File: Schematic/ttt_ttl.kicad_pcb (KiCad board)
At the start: 2 copper layers, 79.8 x 129.5 mm, 80 parts, among them J1 Conn_01x01, J2 Conn_01x01, SW1 SW_Push, SW10 SW_Push, SW2 SW_Push, SW3 SW_Push, SW4 SW_Push, SW5 SW_Push, SW6 SW_Push, SW7 SW_Push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

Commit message: Thanks to Ken Yap, I modified the project to optionally allow the board to move first.
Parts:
- added R13: 10K, Resistor_THT:R_Axial_DIN0207_L6.3mm_D2.5mm_P7.62mm_Horizontal, F.Cu at (101.5, 120.9)
- added SW11: DPDTx2, Package_DIP:DIP-6_W7.62mm, F.Cu at (94.3, 112.6)
- moved R37 4.16 mm to (94.1, 139.1)
- moved D19 4.15 mm to (100.6, 135.4)
- moved D20 3.90 mm to (94.9, 135.4)
- moved R38 3.44 mm to (94.0, 142.5)
- moved U11 3.19 mm to (93.7, 121.0)
- moved C2 2.86 mm to (100.1, 146.0)
- moved R41 2.74 mm to (94.7, 146.0)
- moved U13 2.42 mm to (67.9, 139.0)
- moved C1 1.61 mm to (89.9, 150.9)
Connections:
- U10 pad 26: Lo -> Net-(R13-Pad2)
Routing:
- net Net-(R13-Pad2): track 0.00 -> 61.4 mm
- net Move1: track 123.9 -> 176.3 mm
- net User9: track 72.4 -> 94.9 mm, vias 1 -> 0
- net Newstate3: track 30.8 -> 51.1 mm, vias 1 -> 0
- net Net-(U10-Pad18): track 63.3 -> 45.5 mm
- net Clk: track 362.0 -> 378.6 mm
- net Move4: track 104.8 -> 92.2 mm, vias 0 -> 1
- net Hi: track 582.0 -> 594.5 mm
- net Reset: track 400.0 -> 388.3 mm
- net Move7: track 51.5 -> 62.8 mm, vias 0 -> 1
- net Net-(R38-Pad1): track 24.1 -> 33.3 mm
- net Move2: track 114.4 -> 105.6 mm
- net User3: track 139.4 -> 132.2 mm
- net Newstate0: track 28.3 -> 33.6 mm
- net Net-(R4-Pad1): track 34.1 -> 28.8 mm
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
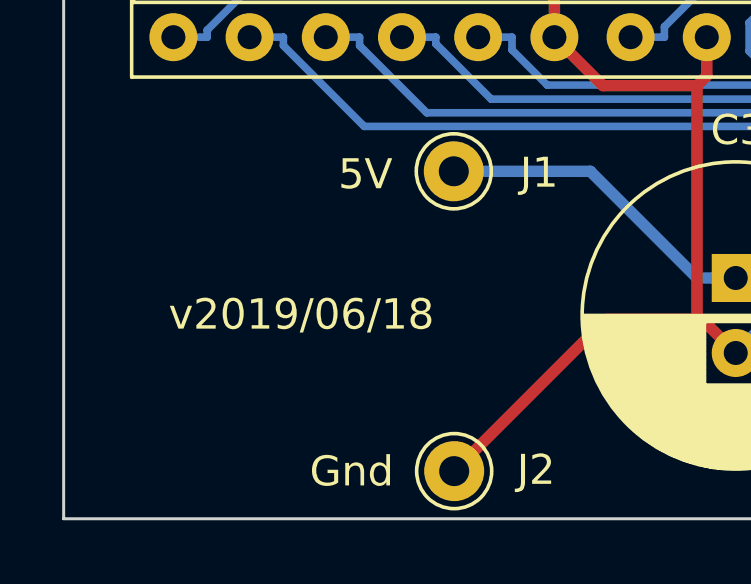
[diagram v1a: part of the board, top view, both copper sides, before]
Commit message: Updated the PCB version number.
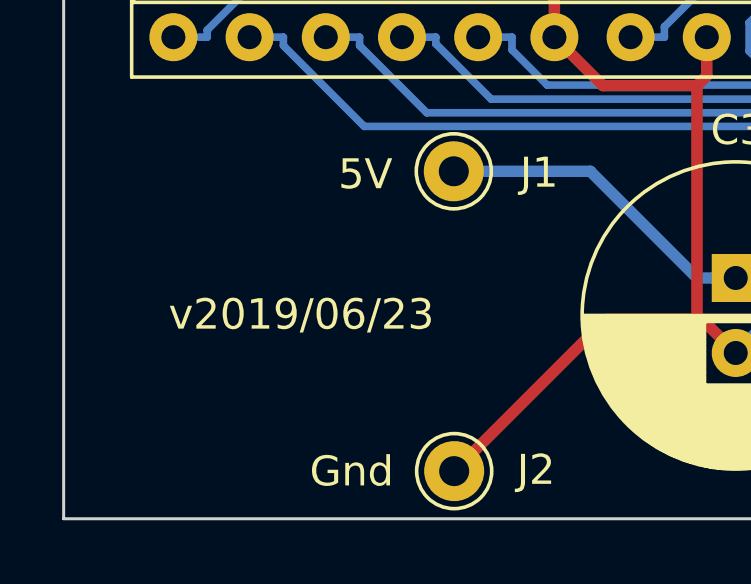
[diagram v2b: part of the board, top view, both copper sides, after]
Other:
- board text added: "v2019/06/23"
- board text removed: "v2019/06/18"
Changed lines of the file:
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@@
     (effects (font (size 1 1) (thickness 0.15)))
   )
-  (gr_text v2019/06/18 (at 32.0548 146.3548) (layer F.SilkS)
+  (gr_text v2019/06/23 (at 32.0548 146.3548) (layer F.SilkS)
     (effects (font (size 1.016 1.016) (thickness 0.254)))
   )
